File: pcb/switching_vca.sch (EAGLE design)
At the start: 8 parts, among them IC1 LF353D, IC2 4053D, Q1 MOSFET-PCHANNELSMD

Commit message: added some simulations
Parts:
- removed IC1: LF353D, linear:LF353D
- removed IC2: 4053D, 40xx:4053D
- added D1: (no value), SparkFun:DIODESOT23
- added Q2: SST5484, transistor-fet:SST5484
- added R4: (no value), SparkFun:RESISTOR0603-RES
- added U1: LM393, SparkFun:LM393
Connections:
- removed net N$2: C1.2, IC1A.-IN, R1.1, R2.2
- removed net SAW: C2.1, IC1A.OUT, IC1B.-IN, Q1.G
- new net N$: C2.1, Q1.G, U1G2.OUT
- new net SAW1: C1.2, R1.1, R2.2, U1G1.+IN, U1G2.-IN
- net CV_IN1: now also U1G1.-IN; no longer IC1B.+IN
- net GND: now also R4.1; no longer IC2A.INH, IC2A.X0, IC2A.Y0, IC2A.Z0
- net IN1: now also Q2.D; no longer IC2A.X1
- net N$3: now also D1.C, U1G1.OUT; no longer IC1P.V+
- net N$4: now also U1G2.+IN; no longer IC1A.+IN
- net N$5: now also D1.A, Q2.G; no longer IC1P.V-
- net N$6: now also Q2.S, R4.2; no longer IC1B.OUT, IC2A.A
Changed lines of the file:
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@@
 <setting verticaltext="up"/>
 </settings>
-<grid distance="0.1" unitdist="inch" unit="inch" style="lines" multiple="1" display="yes" altdistance="0.01" altunitdist="inch" altunit="inch"/>
+<grid distance="0.1" unitdist="inch" unit="inch" style="lines" multiple="1" display="no" altdistance="0.01" altunitdist="inch" altunit="inch"/>
 <layers>
 <layer number="1" name="Top" color="4" fill="1" visible="no" active="no"/>
@@
 <parts>
 <part name="FRAME1" library="SparkFun" deviceset="FRAME-LETTER" device=""/>
-<part name="IC1" library="linear" deviceset="LF353" device="D"/>
 <part name="C1" library="SparkFun" deviceset="CAP" device="1210"/>
 <part name="P+1" library="supply1" deviceset="+12V" device=""/>
@@
 <part name="P+2" library="supply1" deviceset="+5V" device=""/>
 <part name="Q1" library="SparkFun" deviceset="MOSFET-PCHANNEL" device="SMD"/>
-<part name="IC2" library="40xx" deviceset="4053" device="D"/>
+<part name="P-1" library="supply1" deviceset="-12V" device=""/>
+<part name="P+3" library="supply1" deviceset="+12V" device=""/>
+<part name="Q2" library="transistor-fet" deviceset="?548*" device="SST" technology="4"/>
+<part name="D1" library="SparkFun" deviceset="DIODE" device="SOT23"/>
+<part name="R4" library="SparkFun" deviceset="RESISTOR" device="0603-RES"/>
 <part name="GND3" library="supply1" deviceset="GND" device=""/>
+<part name="U1" library="SparkFun" deviceset="LM393" device=""/>
 </parts>
 <sheets>
@@
 <instance part="FRAME1" gate="G$1" x="0" y="0"/>
 <instance part="FRAME1" gate="G$2" x="147.32" y="0"/>
-<instance part="IC1" gate="A" x="48.26" y="162.56"/>
-<instance part="IC1" gate="B" x="83.82" y="165.1"/>
 <instance part="C1" gate="G$1" x="17.78" y="152.4" rot="R180"/>
 <instance part="P+1" gate="1" x="12.7" y="182.88"/>
@@
 <instance part="P+2" gate="1" x="20.32" y="180.34"/>
 <instance part="Q1" gate="G$1" x="27.94" y="139.7" rot="R180"/>
-<instance part="IC1" gate="P" x="83.82" y="165.1"/>
-<instance part="IC2" gate="A" x="139.7" y="149.86"/>
-<instance part="GND3" gate="1" x="119.38" y="132.08"/>
+<instance part="P-1" gate="1" x="81.28" y="152.4"/>
+<instance part="P+3" gate="1" x="81.28" y="180.34"/>
+<instance part="Q2" gate="G$1" x="121.92" y="167.64"/>
+<instance part="D1" gate="G$1" x="101.6" y="165.1" rot="R180"/>
+<instance part="R4" gate="G$1" x="127" y="154.94" rot="R90"/>
+<instance part="GND3" gate="1" x="127" y="142.24"/>
+<instance part="U1" gate="G1" x="81.28" y="165.1"/>
+<instance part="U1" gate="G2" x="48.26" y="162.56"/>
 </instances>
 <busses>
@@
 <wire x1="12.7" y1="180.34" x2="12.7" y2="175.26" width="0.1524" layer="91"/>
 </segment>
-</net>
-<net name="N$2" class="0">
+<segment>
+<pinref part="P+3" gate="1" pin="+12V"/>
+<wire x1="81.28" y1="177.8" x2="81.28" y2="170.18" width="0.1524" layer="91"/>
+</segment>
+</net>
+<net name="SAW1" class="0">
 <segment>
 <pinref part="R1" gate="G$1" pin="1"/>
@@
 <pinref part="C1" gate="G$1" pin="2"/>
 <wire x1="17.78" y1="160.02" x2="17.78" y2="154.94" width="0.1524" layer="91"/>
-<pinref part="IC1" gate="A" pin="-IN"/>
 <wire x1="17.78" y1="160.02" x2="27.94" y2="160.02" width="0.1524" layer="91"/>
 <junction x="17.78" y="160.02"/>
@@
 <wire x1="27.94" y1="160.02" x2="27.94" y2="157.48" width="0.1524" layer="91"/>
 <junction x="27.94" y="160.02"/>
+<pinref part="U1" gate="G2" pin="-IN"/>
+<label x="22.86" y="160.02" size="1.778" layer="95"/>
+</segment>
+<segment>
+<pinref part="U1" gate="G1" pin="+IN"/>
+<wire x1="76.2" y1="162.56" x2="66.04" y2="162.56" width="0.1524" layer="91"/>
+<label x="66.04" y="162.56" size="1.778" layer="95"/>
 </segment>
 </net>
@@
 </segment>
 <segment>
-<pinref part="IC2" gate="A" pin="INH"/>
-<wire x1="127" y1="142.24" x2="119.38" y2="142.24" width="0.1524" layer="91"/>
-<wire x1="119.38" y1="142.24" x2="119.38" y2="134.62" width="0.1524" layer="91"/>
+<pinref part="R4" gate="G$1" pin="1"/>
+<wire x1="127" y1="149.86" x2="127" y2="144.78" width="0.1524" layer="91"/>
 <pinref part="GND3" gate="1" pin="GND"/>
-<wire x1="119.38" y1="142.24" x2="119.38" y2="149.86" width="0.1524" layer="91"/>
-<junction x="119.38" y="142.24"/>
-<pinref part="IC2" gate="A" pin="Z0"/>
-<wire x1="119.38" y1="149.86" x2="127" y2="149.86" width="0.1524" layer="91"/>
-<wire x1="119.38" y1="149.86" x2="119.38" y2="157.48" width="0.1524" layer="91"/>
-<junction x="119.38" y="149.86"/>
-<pinref part="IC2" gate="A" pin="Y0"/>
-<wire x1="119.38" y1="157.48" x2="127" y2="157.48" width="0.1524" layer="91"/>
-<wire x1="119.38" y1="157.48" x2="119.38" y2="165.1" width="0.1524" layer="91"/>
-<junction x="119.38" y="157.48"/>
-<pinref part="IC2" gate="A" pin="X0"/>
-<wire x1="119.38" y1="165.1" x2="127" y2="165.1" width="0.1524" layer="91"/>
 </segment>
 </net>
@@
 </segment>
 </net>
-<net name="SAW" class="0">
-<segment>
-<pinref part="IC1" gate="A" pin="OUT"/>
+<net name="N$" class="0">
+<segment>
 <wire x1="55.88" y1="162.56" x2="60.96" y2="162.56" width="0.1524" layer="91"/>
 <wire x1="60.96" y1="162.56" x2="60.96" y2="139.7" width="0.1524" layer="91"/>
@@
 <wire x1="60.96" y1="175.26" x2="60.96" y2="162.56" width="0.1524" layer="91"/>
 <junction x="60.96" y="162.56"/>
-<wire x1="60.96" y1="162.56" x2="76.2" y2="162.56" width="0.1524" layer="91"/>
-<label x="71.12" y="162.56" size="1.778" layer="95"/>
 <pinref part="Q1" gate="G$1" pin="G"/>
-<pinref part="IC1" gate="B" pin="-IN"/>
+<pinref part="U1" gate="G2" pin="OUT"/>
 </segment>
 </net>
@@
 <wire x1="38.1" y1="175.26" x2="38.1" y2="165.1" width="0.1524" layer="91"/>
 <junction x="38.1" y="175.26"/>
-<pinref part="IC1" gate="A" pin="+IN"/>
 <wire x1="38.1" y1="165.1" x2="40.64" y2="165.1" width="0.1524" layer="91"/>
+<pinref part="U1" gate="G2" pin="+IN"/>
 </segment>
 </net>
 <net name="CV_IN1" class="0">
 <segment>
-<pinref part="IC1" gate="B" pin="+IN"/>
 <wire x1="76.2" y1="167.64" x2="68.58" y2="167.64" width="0.1524" layer="91"/>
 <label x="66.04" y="167.64" size="1.778" layer="95"/>
+<pinref part="U1" gate="G1" pin="-IN"/>
+</segment>
+</net>
+<net name="-12V" class="0">
+<segment>
+<pinref part="P-1" gate="1" pin="-12V"/>
+<wire x1="81.28" y1="157.48" x2="81.28" y2="154.94" width="0.1524" layer="91"/>
 </segment>
 </net>
 <net name="N$3" class="0">
 <segment>
-<pinref part="IC1" gate="P" pin="V+"/>
-<wire x1="83.82" y1="175.26" x2="83.82" y2="172.72" width="0.1524" layer="91"/>
+<pinref part="D1" gate="G$1" pin="C"/>
+<wire x1="91.44" y1="165.1" x2="99.06" y2="165.1" width="0.1524" layer="91"/>
+<pinref part="U1" gate="G1" pin="OUT"/>
 </segment>
 </net>
 <net name="N$5" class="0">
 <segment>
-<pinref part="IC1" gate="P" pin="V-"/>
-<wire x1="83.82" y1="157.48" x2="83.82" y2="154.94" width="0.1524" layer="91"/>
+<pinref part="D1" gate="G$1" pin="A"/>
+<pinref part="Q2" gate="G$1" pin="G"/>
+<wire x1="104.14" y1="165.1" x2="116.84" y2="165.1" width="0.1524" layer="91"/>
+</segment>
+</net>
+<net name="IN1" class="0">
+<segment>
+<pinref part="Q2" gate="G$1" pin="D"/>
+<wire x1="127" y1="170.18" x2="127" y2="175.26" width="0.1524" layer="91"/>
+<wire x1="127" y1="175.26" x2="106.68" y2="175.26" width="0.1524" layer="91"/>
+<label x="106.68" y="175.26" size="1.778" layer="95"/>
 </segment>
 </net>
 <net name="N$6" class="0">
 <segment>
-<pinref part="IC1" gate="B" pin="OUT"/>
-<wire x1="91.44" y1="165.1" x2="106.68" y2="165.1" width="0.1524" layer="91"/>
-<wire x1="106.68" y1="165.1" x2="106.68" y2="139.7" width="0.1524" layer="91"/>
-<pinref part="IC2" gate="A" pin="A"/>
-<wire x1="106.68" y1="139.7" x2="127" y2="139.7" width="0.1524" layer="91"/>
-</segment>
-</net>
-<net name="IN1" class="0">
-<segment>
-<pinref part="IC2" gate="A" pin="X1"/>
-<wire x1="127" y1="162.56" x2="124.46" y2="162.56" width="0.1524" layer="91"/>
-<wire x1="124.46" y1="162.56" x2="124.46" y2="172.72" width="0.1524" layer="91"/>
-<wire x1="124.46" y1="172.72" x2="104.14" y2="172.72" width="0.1524" layer="91"/>
-<label x="104.14" y="172.72" size="1.778" layer="95"/>
-</segment>
-</net>
+<pinref part="Q2" gate="G$1" pin="S"/>
+<pinref part="R4" gate="G$1" pin="2"/>
+<wire x1="127" y1="165.1" x2="127" y2="160.02" width="0.1524" layer="91"/>
+</segment>
+</net>

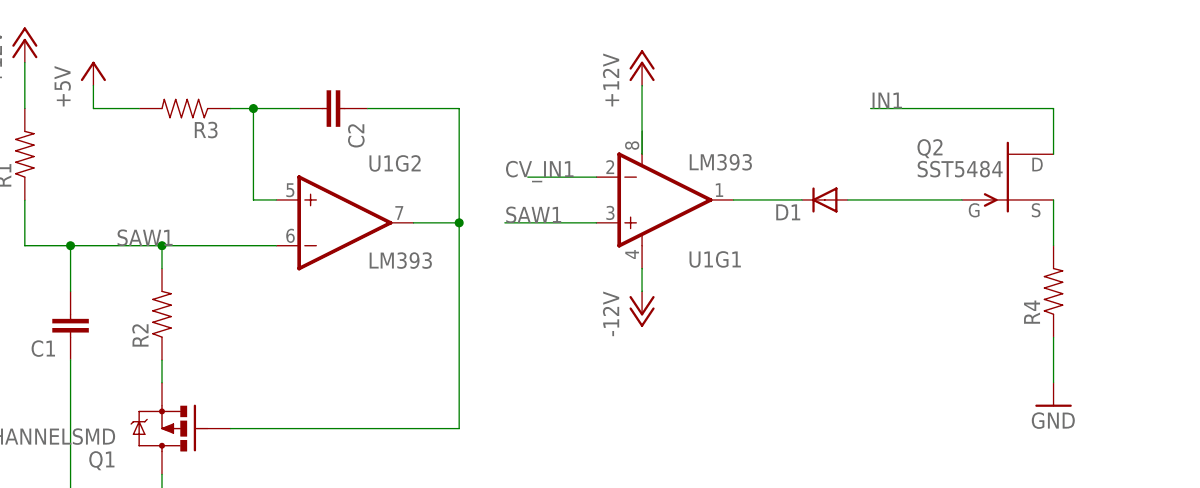
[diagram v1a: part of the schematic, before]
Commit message: found a fast comparator so remove the level conversion stage of the switch simulation
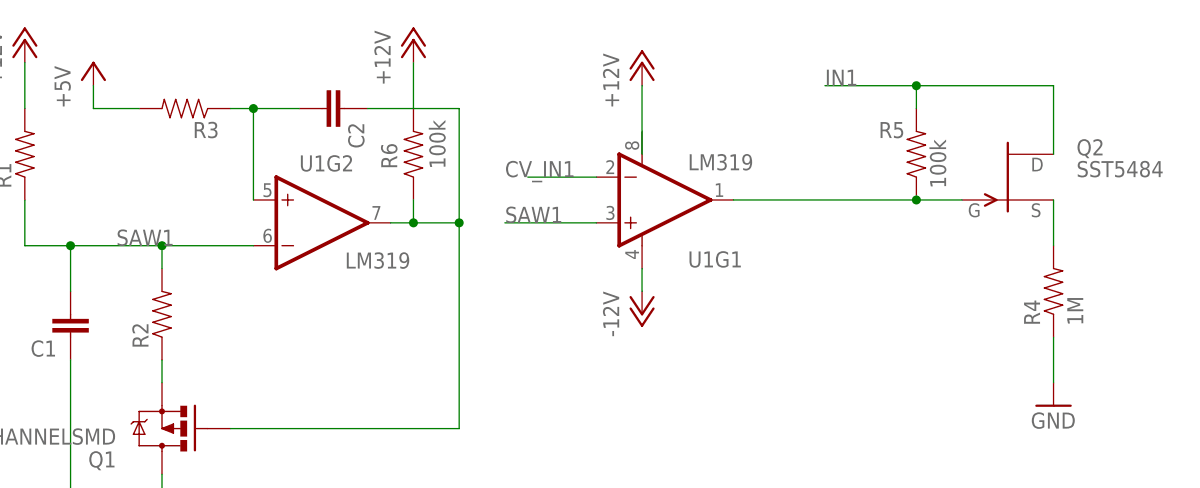
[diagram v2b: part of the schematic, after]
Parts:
- removed D1: (no value), SparkFun:DIODESOT23
- added R5, R6: 100k, SparkFun:RESISTOR0603-RES
- R4: value (none) -> 1M
- U1: value LM393 -> LM319
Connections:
- removed net N$5: D1.A, Q2.G
- net +12V: now also R6.2
- net IN1: now also R5.2
- net N$: now also R6.1
- net N$3: now also Q2.G, R5.1; no longer D1.C
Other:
- moved on the sheet: U1G2
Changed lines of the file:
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@@
 <part name="P+3" library="supply1" deviceset="+12V" device=""/>
 <part name="Q2" library="transistor-fet" deviceset="?548*" device="SST" technology="4"/>
-<part name="D1" library="SparkFun" deviceset="DIODE" device="SOT23"/>
-<part name="R4" library="SparkFun" deviceset="RESISTOR" device="0603-RES"/>
+<part name="R4" library="SparkFun" deviceset="RESISTOR" device="0603-RES" value="1M"/>
 <part name="GND3" library="supply1" deviceset="GND" device=""/>
-<part name="U1" library="SparkFun" deviceset="LM393" device=""/>
+<part name="U1" library="SparkFun" deviceset="LM393" device="" value="LM319"/>
+<part name="R5" library="SparkFun" deviceset="RESISTOR" device="0603-RES" value="100k"/>
+<part name="R6" library="SparkFun" deviceset="RESISTOR" device="0603-RES" value="100k"/>
+<part name="P+4" library="supply1" deviceset="+12V" device=""/>
 </parts>
 <sheets>
@@
 <instance part="P-1" gate="1" x="81.28" y="152.4"/>
 <instance part="P+3" gate="1" x="81.28" y="180.34"/>
-<instance part="Q2" gate="G$1" x="121.92" y="167.64"/>
-<instance part="D1" gate="G$1" x="101.6" y="165.1" rot="R180"/>
+<instance part="Q2" gate="G$1" x="121.92" y="167.64" smashed="yes">
+<attribute name="NAME" x="129.54" y="170.053" size="1.778" layer="95"/>
+<attribute name="VALUE" x="129.54" y="167.64" size="1.778" layer="96"/>
+</instance>
 <instance part="R4" gate="G$1" x="127" y="154.94" rot="R90"/>
 <instance part="GND3" gate="1" x="127" y="142.24"/>
 <instance part="U1" gate="G1" x="81.28" y="165.1"/>
-<instance part="U1" gate="G2" x="48.26" y="162.56"/>
+<instance part="U1" gate="G2" x="45.72" y="162.56" smashed="yes">
+<attribute name="NAME" x="43.18" y="168.275" size="1.778" layer="95"/>
+<attribute name="VALUE" x="48.26" y="157.48" size="1.778" layer="96"/>
+</instance>
+<instance part="R5" gate="G$1" x="111.76" y="170.18" smashed="yes" rot="R90">
+<attribute name="NAME" x="110.49" y="173.7614" size="1.778" layer="95" rot="R180"/>
+<attribute name="VALUE" x="115.062" y="166.37" size="1.778" layer="96" rot="R90"/>
+</instance>
+<instance part="R6" gate="G$1" x="55.88" y="170.18" smashed="yes" rot="R90">
+<attribute name="NAME" x="52.2986" y="171.45" size="1.778" layer="95" rot="R270"/>
+<attribute name="VALUE" x="57.658" y="173.99" size="1.778" layer="96" rot="R270"/>
+</instance>
+<instance part="P+4" gate="1" x="55.88" y="182.88"/>
 </instances>
 <busses>
@@
 <wire x1="81.28" y1="177.8" x2="81.28" y2="170.18" width="0.1524" layer="91"/>
 </segment>
+<segment>
+<pinref part="P+4" gate="1" pin="+12V"/>
+<pinref part="R6" gate="G$1" pin="2"/>
+<wire x1="55.88" y1="180.34" x2="55.88" y2="175.26" width="0.1524" layer="91"/>
+</segment>
 </net>
 <net name="SAW1" class="0">
@@
 <junction x="17.78" y="160.02"/>
 <pinref part="R2" gate="G$1" pin="2"/>
-<wire x1="27.94" y1="160.02" x2="40.64" y2="160.02" width="0.1524" layer="91"/>
+<wire x1="27.94" y1="160.02" x2="38.1" y2="160.02" width="0.1524" layer="91"/>
 <wire x1="27.94" y1="160.02" x2="27.94" y2="157.48" width="0.1524" layer="91"/>
 <junction x="27.94" y="160.02"/>
@@
 <net name="N$" class="0">
 <segment>
-<wire x1="55.88" y1="162.56" x2="60.96" y2="162.56" width="0.1524" layer="91"/>
+<wire x1="60.96" y1="175.26" x2="60.96" y2="162.56" width="0.1524" layer="91"/>
 <wire x1="60.96" y1="162.56" x2="60.96" y2="139.7" width="0.1524" layer="91"/>
 <wire x1="60.96" y1="139.7" x2="35.56" y2="139.7" width="0.1524" layer="91"/>
+<pinref part="Q1" gate="G$1" pin="G"/>
 <pinref part="C2" gate="G$1" pin="1"/>
-<wire x1="50.8" y1="175.26" x2="60.96" y2="175.26" width="0.1524" layer="91"/>
-<wire x1="60.96" y1="175.26" x2="60.96" y2="162.56" width="0.1524" layer="91"/>
+<wire x1="60.96" y1="175.26" x2="50.8" y2="175.26" width="0.1524" layer="91"/>
+<pinref part="U1" gate="G2" pin="OUT"/>
+<wire x1="53.34" y1="162.56" x2="55.88" y2="162.56" width="0.1524" layer="91"/>
 <junction x="60.96" y="162.56"/>
-<pinref part="Q1" gate="G$1" pin="G"/>
-<pinref part="U1" gate="G2" pin="OUT"/>
+<pinref part="R6" gate="G$1" pin="1"/>
+<wire x1="55.88" y1="162.56" x2="60.96" y2="162.56" width="0.1524" layer="91"/>
+<wire x1="55.88" y1="165.1" x2="55.88" y2="162.56" width="0.1524" layer="91"/>
+<junction x="55.88" y="162.56"/>
 </segment>
 </net>
@@
 <wire x1="38.1" y1="175.26" x2="38.1" y2="165.1" width="0.1524" layer="91"/>
 <junction x="38.1" y="175.26"/>
-<wire x1="38.1" y1="165.1" x2="40.64" y2="165.1" width="0.1524" layer="91"/>
 <pinref part="U1" gate="G2" pin="+IN"/>
 </segment>
@@
 <net name="N$3" class="0">
 <segment>
-<pinref part="D1" gate="G$1" pin="C"/>
-<wire x1="91.44" y1="165.1" x2="99.06" y2="165.1" width="0.1524" layer="91"/>
+<wire x1="91.44" y1="165.1" x2="111.76" y2="165.1" width="0.1524" layer="91"/>
 <pinref part="U1" gate="G1" pin="OUT"/>
-</segment>
-</net>
-<net name="N$5" class="0">
-<segment>
-<pinref part="D1" gate="G$1" pin="A"/>
 <pinref part="Q2" gate="G$1" pin="G"/>
-<wire x1="104.14" y1="165.1" x2="116.84" y2="165.1" width="0.1524" layer="91"/>
-</segment>
-</net>
-<net name="IN1" class="0">
-<segment>
-<pinref part="Q2" gate="G$1" pin="D"/>
-<wire x1="127" y1="170.18" x2="127" y2="175.26" width="0.1524" layer="91"/>
-<wire x1="127" y1="175.26" x2="106.68" y2="175.26" width="0.1524" layer="91"/>
-<label x="106.68" y="175.26" size="1.778" layer="95"/>
+<pinref part="R5" gate="G$1" pin="1"/>
+<wire x1="111.76" y1="165.1" x2="116.84" y2="165.1" width="0.1524" layer="91"/>
+<junction x="111.76" y="165.1"/>
 </segment>
 </net>
@@
 </segment>
 </net>
+<net name="IN1" class="0">
+<segment>
+<pinref part="Q2" gate="G$1" pin="D"/>
+<wire x1="127" y1="170.18" x2="127" y2="177.8" width="0.1524" layer="91"/>
+<wire x1="127" y1="177.8" x2="111.76" y2="177.8" width="0.1524" layer="91"/>
+<label x="101.6" y="177.8" size="1.778" layer="95"/>
+<pinref part="R5" gate="G$1" pin="2"/>
+<wire x1="111.76" y1="177.8" x2="101.6" y2="177.8" width="0.1524" layer="91"/>
+<wire x1="111.76" y1="175.26" x2="111.76" y2="177.8" width="0.1524" layer="91"/>
+<junction x="111.76" y="177.8"/>
+</segment>
+</net>
